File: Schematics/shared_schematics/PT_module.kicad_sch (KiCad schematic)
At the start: 7 parts

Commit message: add requested changes for PR
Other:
- note added: "0.1 µF in 0805 for low parasitics and fast HF response; 10 µF in 1206 for larger bulk charge."
- note added: "package choice also affected by DC Bias Effect, higher cap MLCCs in smaller packages lose a significant pct of their effective capacitance."
- note added: "parallel decoupling circuit at the PT connector positive to suppress fast and slow transients and provide effective decoupling. 0.1 µF for high-frequency noise, 10 µF for bulk transient suppression."
- note added: "place the 0.1uF closer to the SOL input due to faster responsiveness (HF filter) the larger cap handles LF, therefore slightly less sensitive to placement"
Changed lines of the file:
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@@
+		)
+	)
+	(text "parallel decoupling circuit at the PT connector positive\nto suppress fast and slow transients and provide effective decoupling.\n\n0.1 µF for high-frequency noise, 10 µF for bulk transient suppression."
+		(exclude_from_sim no)
+		(at 118.364 120.142 0)
+		(effects
+			(font
+				(size 1.016 1.016)
+				(color 0 0 0 1)
+			)
+		)
+	)
+	(text "place the 0.1uF closer to the SOL input due to faster responsiveness (HF filter)\nthe larger cap handles LF, therefore slightly less sensitive to placement\n"
+		(exclude_from_sim no)
+		(at 119.38 136.652 0)
+		(effects
+			(font
+				(size 1.27 1.27)
+				(color 0 0 0 1)
+			)
+		)
+	)
+	(text "package choice also affected by DC Bias Effect, higher cap MLCCs \nin smaller packages lose a significant pct of their effective\ncapacitance."
+		(exclude_from_sim no)
+		(at 168.91 129.54 0)
+		(effects
+			(font
+				(size 1.016 1.016)
+				(color 0 0 0 1)
+			)
+		)
+	)
+	(text "0.1 µF in 0805 for low parasitics and fast HF response; \n10 µF in 1206 for larger bulk charge."
+		(exclude_from_sim no)
+		(at 118.364 128.778 0)
+		(effects
+			(font
+				(size 1.016 1.016)
+				(color 0 0 0 1)
+			)
 		)
 	)
@@
 		)
 	)
+	(sheet_instances
+		(path "/"
+			(page "1")
+		)
+	)

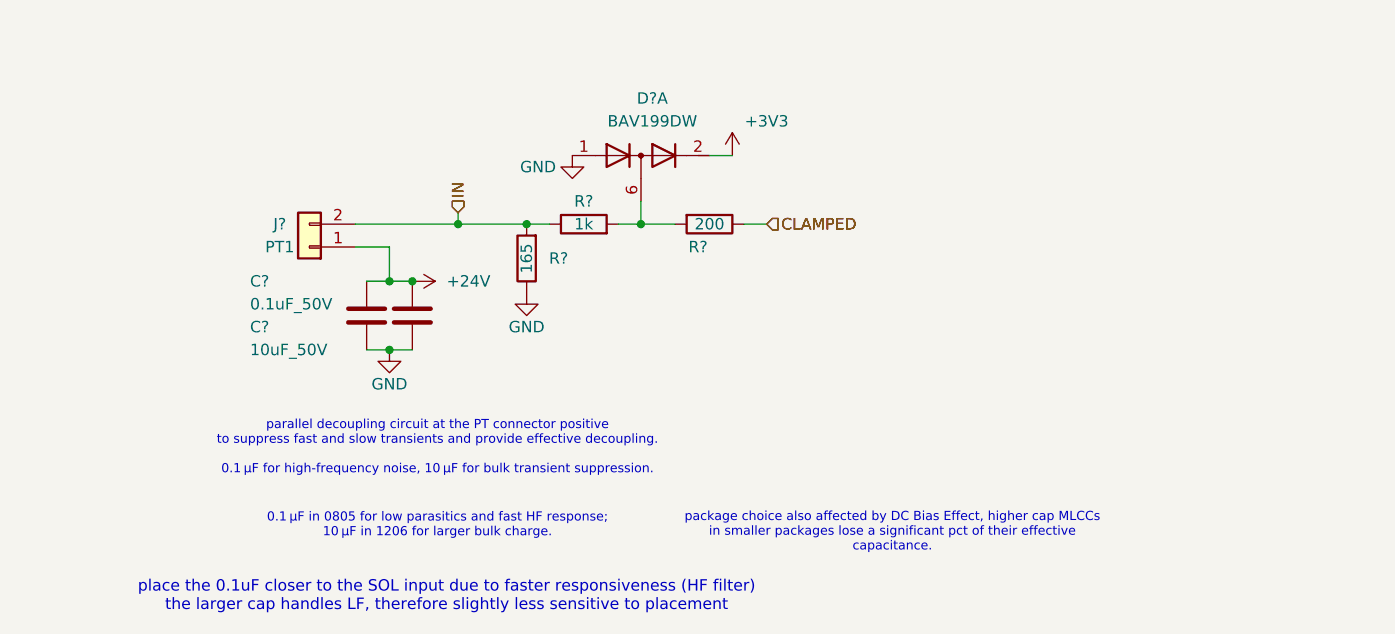
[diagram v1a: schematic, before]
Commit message: add all circuitry and missing datasheets
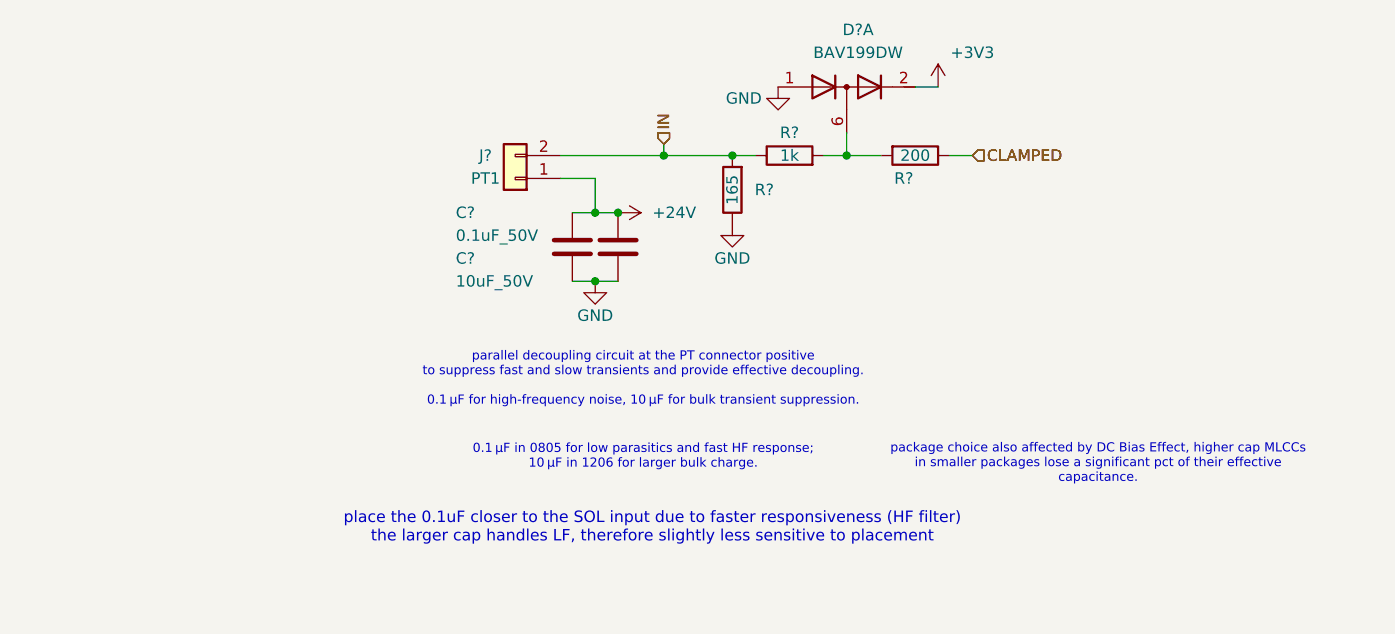
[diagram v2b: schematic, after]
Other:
- moved on the sheet: C?, D?A, J?, R?

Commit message: pin assignments verified
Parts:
- J?: footprint CONNS:CONN02_530470260_MOL -> S02B_PASK_2:CONN2_S02B-PASK-2_JST
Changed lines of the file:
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@@
 			)
 		)
-		(property "Footprint" "CONNS:CONN02_530470260_MOL"
+		(property "Footprint" "S02B_PASK_2:CONN2_S02B-PASK-2_JST"
 			(at 127 90.17 0)
 			(effects

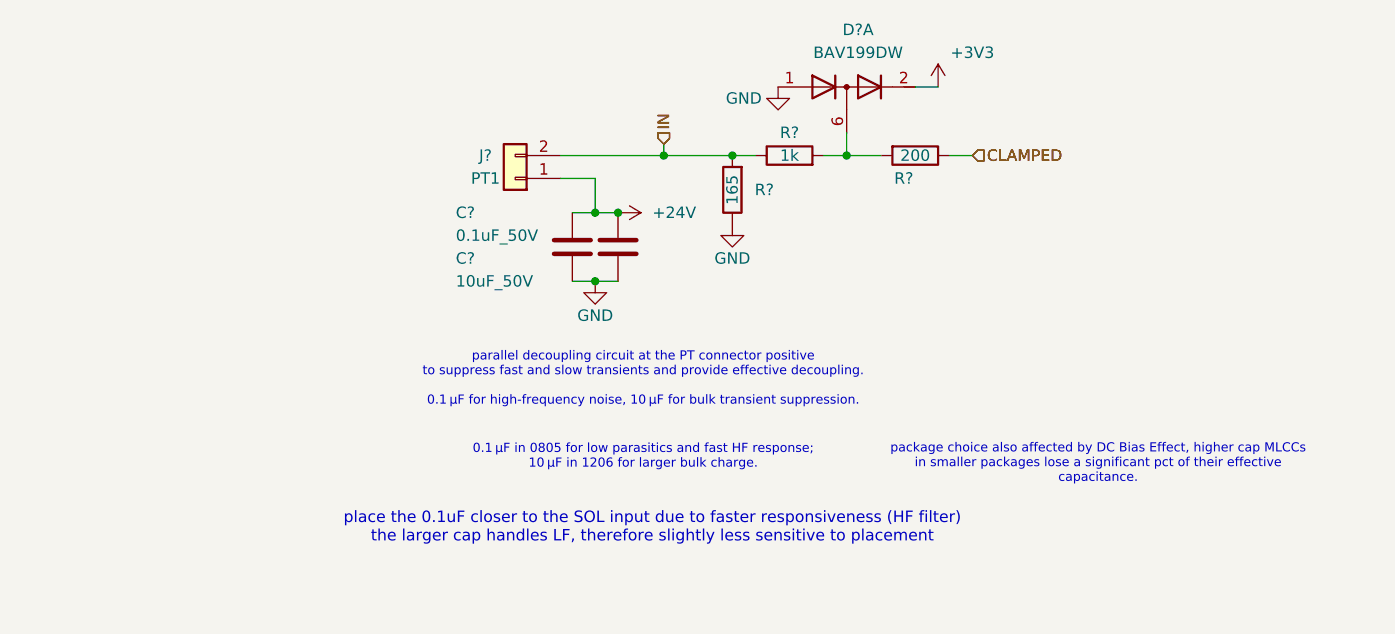
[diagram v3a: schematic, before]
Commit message: finish layout
- model paths need to be fixed
- waiting for confirmation for shared folders
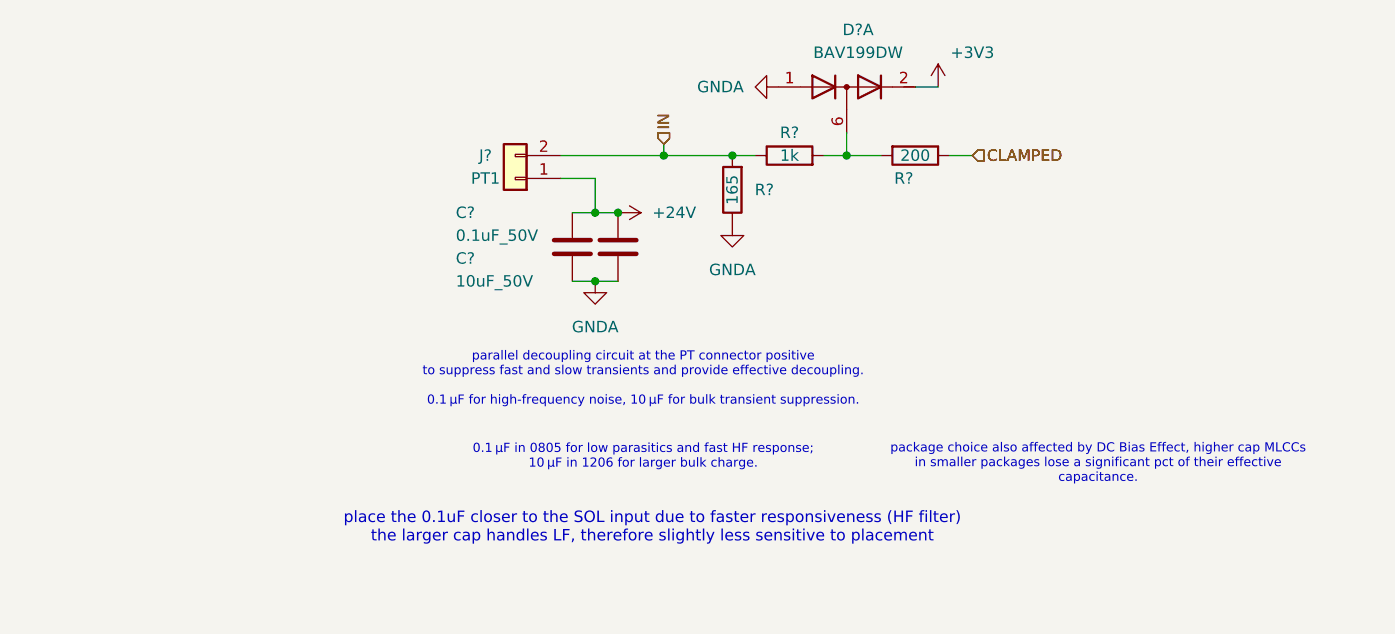
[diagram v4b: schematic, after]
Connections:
- net GND renamed GNDA

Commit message: add power switching for PTs (schematic only)
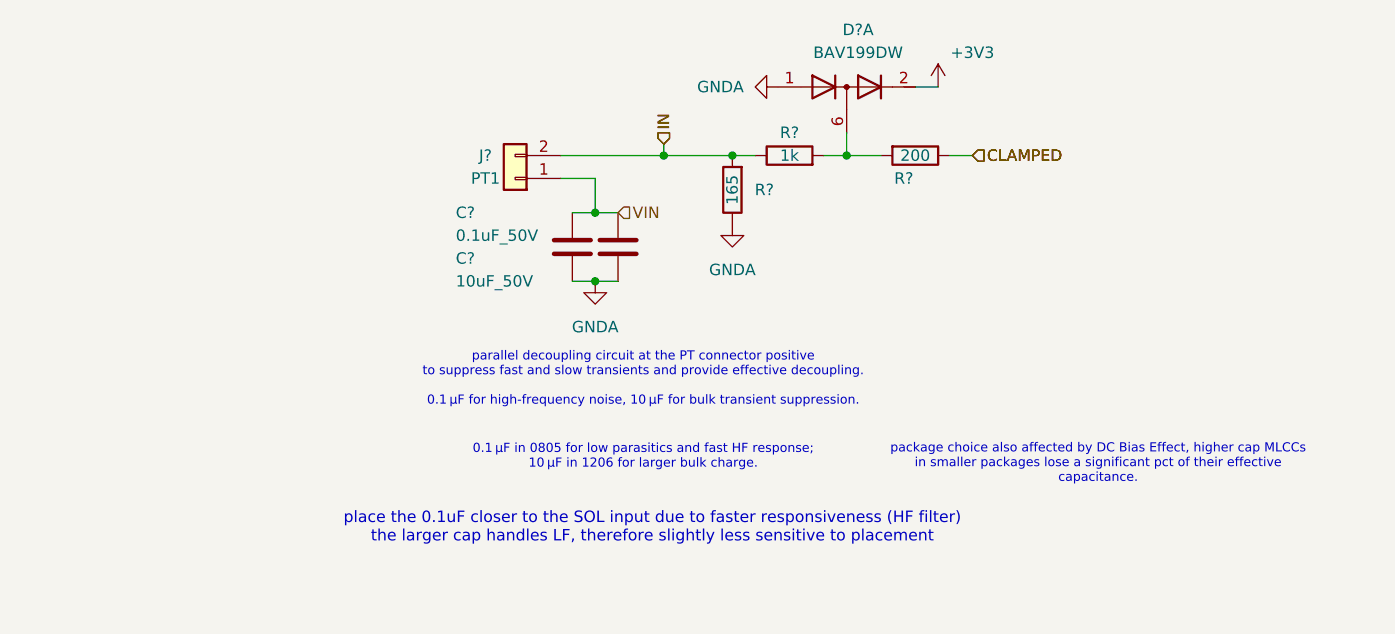
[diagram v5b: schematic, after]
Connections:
- net +24V renamed VIN
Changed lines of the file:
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@@
-	)
-	(junction
-		(at 138.43 93.98)
-		(diameter 0)
-		(color 0 0 0 0)
 	)
 	(junction
@@
 		)
 	)
+	(hierarchical_label "VIN"
+		(shape input)
+		(at 138.43 93.98 0)
+		(fields_autoplaced yes)
+		(effects
+			(font
+				(size 1.27 1.27)
+			)
+			(justify left)
+		)
+	)
 	(hierarchical_label "IN"
 		(shape input)
@@
 		(dnp no)
 		(fields_autoplaced yes)
-		(property "Reference" "#PWR085"
+		(property "Reference" "#PWR086"
 			(at 135.89 107.95 0)
 			(effects
@@
 	)
 	(symbol
-		(lib_id "power:+24V")
-		(at 138.43 93.98 270)
-		(unit 1)
-		(exclude_from_sim no)
-		(in_bom yes)
-		(on_board yes)
-		(dnp no)
-		(fields_autoplaced yes)
-		(property "Reference" "#PWR?"
-			(at 134.62 93.98 0)
-			(effects
-				(font
-					(size 1.27 1.27)
-				)
-				(hide yes)
-			)
-		)
-		(property "Value" "+24V"
-			(at 142.24 93.9799 90)
-			(effects
-				(font
-					(size 1.27 1.27)
-				)
-				(justify left)
-			)
-		)
-		(property "Footprint" ""
-			(at 138.43 93.98 0)
-			(effects
-				(font
-					(size 1.27 1.27)
-				)
-				(hide yes)
-			)
-		)
-		(property "Datasheet" ""
-			(at 138.43 93.98 0)
-			(effects
-				(font
-					(size 1.27 1.27)
-				)
-				(hide yes)
-			)
-		)
-		(property "Description" "Power symbol creates a global label with name \"+24V\""
-			(at 138.43 93.98 0)
-			(effects
-				(font
-					(size 1.27 1.27)
-				)
-				(hide yes)
-			)
-		)
-		(pin "1"
-		)
-		(instances
-			(project "PT_module"
-				(path "/2c2a8324-b3b2-4288-b95a-2bccf1374493"
-					(reference "#PWR?")
-					(unit 1)
-				)
-			)
-			(project "upper_lc_board"
-				(path "/9b1a1d2a-fad7-4f10-83f3-1f83e9656c75/03f1622b-3dda-4e29-911f-7cc762ec6c20/053ff26d-da11-4577-8dd0-32aaebff2a7b"
-					(reference "#PWR0105")
-					(unit 1)
-				)
-				(path "/9b1a1d2a-fad7-4f10-83f3-1f83e9656c75/03f1622b-3dda-4e29-911f-7cc762ec6c20/3fcdaac5-2869-40f8-b925-cf310375456d"
-					(reference "#PWR0109")
-					(unit 1)
-				)
-			)
-			(project "PT_module"
-				(path "/d63798c4-e363-437e-9012-e4aff32e6642/c6419db7-28a9-4bfa-8244-fc88166c795c/04099e68-2fb2-4ed9-b47f-64e383012a5e"
-					(reference "#PWR088")
-					(unit 1)
-				)
-				(path "/d63798c4-e363-437e-9012-e4aff32e6642/c6419db7-28a9-4bfa-8244-fc88166c795c/b32c9da1-3632-45cf-9fa2-2747a45f88ee"
-					(reference "#PWR084")
-					(unit 1)
-				)
-			)
-		)
-	)
-	(symbol
 		(lib_id "Device:C")
 		(at 133.35 97.79 0)
@@
 		(dnp no)
 		(fields_autoplaced yes)
-		(property "Reference" "#PWR089"
+		(property "Reference" "#PWR090"
 			(at 151.13 101.6 0)
 			(effects
@@
 		(dnp no)
 		(fields_autoplaced yes)
-		(property "Reference" "#PWR0101"
+		(property "Reference" "#PWR0102"
 			(at 149.86 80.01 0)
 			(effects

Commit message: organizational work
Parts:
- C?: value 0.1uF_50V -> 0.1uF
- C?: value 10uF_50V -> 10uF
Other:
- note removed: "0.1 µF in 0805 for low parasitics and fast HF response; 10 µF in 1206 for larger bulk charge."
- note removed: "package choice also affected by DC Bias Effect, higher cap MLCCs in smaller packages lose a significant pct of their effective capacitance."
- note removed: "parallel decoupling circuit at the PT connector positive to suppress fast and slow transients and provide effective decoupling. 0.1 µF for high-frequency noise, 10 µF for bulk transient suppression."
- note removed: "place the 0.1uF closer to the SOL input due to faster responsiveness (HF filter) the larger cap handles LF, therefore slightly less sensitive to placement"
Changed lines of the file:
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@@
-		)
-	)
-	(text "parallel decoupling circuit at the PT connector positive\nto suppress fast and slow transients and provide effective decoupling.\n\n0.1 µF for high-frequency noise, 10 µF for bulk transient suppression."
-		(exclude_from_sim no)
-		(at 141.224 112.522 0)
-		(effects
-			(font
-				(size 1.016 1.016)
-				(color 0 0 0 1)
-			)
-		)
-	)
-	(text "place the 0.1uF closer to the SOL input due to faster responsiveness (HF filter)\nthe larger cap handles LF, therefore slightly less sensitive to placement\n"
-		(exclude_from_sim no)
-		(at 142.24 129.032 0)
-		(effects
-			(font
-				(size 1.27 1.27)
-				(color 0 0 0 1)
-			)
-		)
-	)
-	(text "package choice also affected by DC Bias Effect, higher cap MLCCs \nin smaller packages lose a significant pct of their effective\ncapacitance."
-		(exclude_from_sim no)
-		(at 191.77 121.92 0)
-		(effects
-			(font
-				(size 1.016 1.016)
-				(color 0 0 0 1)
-			)
-		)
-	)
-	(text "0.1 µF in 0805 for low parasitics and fast HF response; \n10 µF in 1206 for larger bulk charge."
-		(exclude_from_sim no)
-		(at 141.224 121.158 0)
-		(effects
-			(font
-				(size 1.016 1.016)
-				(color 0 0 0 1)
-			)
 		)
 	)
@@
 			)
 		)
-		(property "Value" "0.1uF_50V"
+		(property "Value" "0.1uF"
 			(at 120.396 96.52 0)
 			(effects
@@
 			)
 		)
-		(property "Value" "10uF_50V"
+		(property "Value" "10uF"
 			(at 120.396 101.6 0)
 			(effects

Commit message: more organizational work, add shared footprint, model, symbol dirs and clean up individuals
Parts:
- J?: footprint S02B_PASK_2:CONN2_S02B-PASK-2_JST -> ul_B02B-PASK-1:CONN_B02B-PASK-1_JST
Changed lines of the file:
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@@
 		)
 		(instances
+			(project ""
+				(path "/9b1a1d2a-fad7-4f10-83f3-1f83e9656c75/03f1622b-3dda-4e29-911f-7cc762ec6c20/053ff26d-da11-4577-8dd0-32aaebff2a7b"
+					(reference "#PWR086")
+					(unit 1)
+				)
+				(path "/9b1a1d2a-fad7-4f10-83f3-1f83e9656c75/03f1622b-3dda-4e29-911f-7cc762ec6c20/3fcdaac5-2869-40f8-b925-cf310375456d"
+					(reference "#PWR0106")
+					(unit 1)
+				)
+			)
 			(project "lower_lc_board"
 				(path "/d63798c4-e363-437e-9012-e4aff32e6642/c6419db7-28a9-4bfa-8244-fc88166c795c/04099e68-2fb2-4ed9-b47f-64e383012a5e"
@@
 			)
 		)
-		(property "Footprint" "S02B_PASK_2:CONN2_S02B-PASK-2_JST"
+		(property "Footprint" "ul_B02B-PASK-1:CONN_B02B-PASK-1_JST"
 			(at 127 90.17 0)
 			(effects
@@
 			)
 		)
-		(property "Datasheet" "${KIPRJMOD}/../../Datasheets/CONN-530470460.pdf"
+		(property "Datasheet" "${KIPRJMOD}/../../Documentation/conn_jst_B0XB-PASK-1_DS.pdf"
 			(at 127 90.17 0)
 			(effects
@@
 			)
 		)
-		(property "Datasheet" "${KIPRJMOD}/../../Datasheets/BAV199DW-ds30417.pdf"
+		(property "Datasheet" "${KIPRJMOD}/../../Documentation/diode_BAV16WS_DS.pdf"
 			(at 163.83 80.01 0)
 			(effects
@@
 		)
 		(instances
+			(project ""
+				(path "/9b1a1d2a-fad7-4f10-83f3-1f83e9656c75/03f1622b-3dda-4e29-911f-7cc762ec6c20/053ff26d-da11-4577-8dd0-32aaebff2a7b"
+					(reference "#PWR090")
+					(unit 1)
+				)
+				(path "/9b1a1d2a-fad7-4f10-83f3-1f83e9656c75/03f1622b-3dda-4e29-911f-7cc762ec6c20/3fcdaac5-2869-40f8-b925-cf310375456d"
+					(reference "#PWR0108")
+					(unit 1)
+				)
+			)
 			(project "lower_lc_board"
 				(path "/d63798c4-e363-437e-9012-e4aff32e6642/c6419db7-28a9-4bfa-8244-fc88166c795c/04099e68-2fb2-4ed9-b47f-64e383012a5e"
@@
 		(dnp no)
 		(fields_autoplaced yes)
-		(property "Reference" "#PWR0102"
+		(property "Reference" "#PWR0104"
 			(at 149.86 80.01 0)
 			(effects
@@
 		)
 		(instances
+			(project ""
+				(path "/9b1a1d2a-fad7-4f10-83f3-1f83e9656c75/03f1622b-3dda-4e29-911f-7cc762ec6c20/053ff26d-da11-4577-8dd0-32aaebff2a7b"
+					(reference "#PWR0104")
+					(unit 1)
+				)
+				(path "/9b1a1d2a-fad7-4f10-83f3-1f83e9656c75/03f1622b-3dda-4e29-911f-7cc762ec6c20/3fcdaac5-2869-40f8-b925-cf310375456d"
+					(reference "#PWR0105")
+					(unit 1)
+				)
+			)
 			(project "lower_lc_board"
 				(path "/d63798c4-e363-437e-9012-e4aff32e6642/c6419db7-28a9-4bfa-8244-fc88166c795c/04099e68-2fb2-4ed9-b47f-64e383012a5e"

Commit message: routing work
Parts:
- C?: JLCPCB (none) -> C49678
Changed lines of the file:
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@@
+			)
+		)
+		(property "JLCPCB" "C49678"
+			(at 133.35 97.79 0)
+			(effects
+				(font
+					(size 1.27 1.27)
+				)
+				(hide yes)
 			)
 		)
